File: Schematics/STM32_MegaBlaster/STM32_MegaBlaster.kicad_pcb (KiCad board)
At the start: 2 copper layers, 89 parts, among them J1 SD_Card, J2 USB_B, J3 Barrel_Jack, J4 AMP_OUT, J5 LINE_LEVEL_OUT, SW1 PREV, SW2 RAND, SW3 NEXT, SW4 OPTION, SW5 PWR_SWITCH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

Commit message: PCB near complete
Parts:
- removed J5: LINE_LEVEL_OUT, Connectors:PJ320E_3.5mm_Jack
- removed R12, R14: 9.1k, Resistors_THT:R_Axial_DIN0207_L6.3mm_D2.5mm_P7.62mm_Horizontal
- removed R13, R15: 1.2k, Resistors_THT:R_Axial_DIN0207_L6.3mm_D2.5mm_P7.62mm_Horizontal
- removed SW7: GLOBAL_MUTE, Switches:1825115-1
- added ?: , , F.Cu at (186.3, 47.1)
- added C37: 1000uF, Capacitors_THT:CP_Radial_D8.0mm_P2.50mm, F.Cu at (125.1, 36.2)
- added RV1: POT_Dual, Potentiometers:Potentiometer_Alps_RK163_Double_Vertical, F.Cu at (191.6, 116.6)
- C3: footprint Capacitors_THT:C_Axial_L22.0mm_D10.5mm_P27.50mm_Horizontal -> Capacitors_THT:C_Disc_D3.0mm_W1.6mm_P2.50mm
- SW5: value PWR_SWITCH -> POWER
- SW6: value MUTE_SN -> MUTE PSG
- moved C9 144.3 mm to (63.5, 71.8), turned to 180 degrees
- moved SW1 141.7 mm to (84.3, 101.7)
- moved C10 140.8 mm to (85.1, 78.7), turned to 270 degrees
- moved U4 135.2 mm to (69.8, 74.3)
- moved C4 133.2 mm to (105.4, 33.7), turned to 180 degrees
- moved U5 129.6 mm to (108.0, 37.5)
- moved R2 126.8 mm to (87.9, 38.7)
- moved R3 126.7 mm to (87.9, 35.4)
- moved C1 124.7 mm to (118.7, 38.7)
- moved C2 122.7 mm to (113.7, 38.7)
- moved C15 118.8 mm to (115.6, 33.7), turned to 180 degrees
- moved C12 118.7 mm to (63.5, 76.8), turned to 180 degrees
- moved C13 116.5 mm to (175.3, 43.2)
- moved J2 112.9 mm to (74.9, 88.3), turned to 180 degrees
- moved C16 110.2 mm to (128.9, 62.2), turned to 180 degrees
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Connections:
- J4 pad 1: GND -> Net-(J4-Pad1)
- J4 pad 2: L_OUT -> Net-(J4-Pad2)
- J4 pad 3: R_OUT -> Net-(J4-Pad3)
- J4 pad 4: Net-(J4-Pad4) -> GND
- U9 pad 3: Net-(SW7-Pad2) -> GND
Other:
- board outline added: 138.4 x 91.4 mm
- board text added: "I"
- board text added: "O"
- board text added: "OFF"
- board text added: "ON"

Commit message: PCB Complete
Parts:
- removed ?: , 
- added G***: LOGO, art:wave3, B.Cu at (154.1, 109.0)
- added G1: LOGO, art:wave1, F.Cu at (80.2, 112.3)
- added G2: LOGO, art:mega_blaster_logo, F.Cu at (71.4, 100.6)
- added G3: LOGO, art:wave2, B.Cu at (86.3, 106.0)
- added G4: LOGO, art:trees, B.Cu at (72.4, 47.8)
- SW6: value MUTE PSG -> MUTE_SN
- VOLUME: renamed from RV1; footprint Potentiometers:Potentiometer_Alps_RK163_Double_Vertical -> Potentiometer_Alps_RK163_Double_Vertical(SWAP)
- moved NEXT 10.8 mm to (116.0, 102.3)
- moved RAND 10.8 mm to (105.2, 102.3)
- moved PREV 10.8 mm to (95.0, 102.3)
- moved PLAYMODE 10.8 mm to (105.2, 111.7)
- moved J1 6.98 mm to (73.0, 48.3)
- moved C10 5.08 mm to (85.1, 73.7)
- moved C11 5.08 mm to (85.1, 68.6)
- moved Y1 5.08 mm to (80.0, 73.7)
- moved C9 3.81 mm to (63.5, 67.9)
- moved U4 3.81 mm to (69.8, 70.5)
- moved C12 3.81 mm to (63.5, 73.0)
- moved C3 2.29 mm to (113.0, 71.1)
- moved U2 2.01 mm to (116.2, 78.7)
- moved C16 1.91 mm to (130.8, 62.2)
- moved C5 1.91 mm to (125.7, 65.4)
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- renumbered SW3 to NEXT, SW4 to PLAYMODE, SW1 to PREV, SW2 to RAND
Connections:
- R3 pad 2: I2C_SCL -> I2C_SDA
- U1 pad 35: I2C_SCL -> I2C_SDA
- U12 pad 4: I2C_SCL -> I2C_SDA
- U5 pad 2: I2C_SCL -> I2C_SDA
- U6 pad 2: I2C_SCL -> I2C_SDA
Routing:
- net +5V: track 0.00 -> 234.1 mm, vias 0 -> 4
- net +3V3: track 0.00 -> 169.9 mm
- net GND: track 0.00 -> 107.3 mm, vias 0 -> 13
- net I2C_SDA: track 0.00 -> 95.2 mm, vias 0 -> 1
- net YM_A0: track 0.00 -> 94.8 mm, vias 0 -> 2
- net I2C_SCL: track 0.00 -> 91.8 mm
- net YM_WR: track 0.00 -> 87.3 mm
- net D6: track 0.00 -> 85.6 mm, vias 0 -> 1
- net D5: track 0.00 -> 85.1 mm, vias 0 -> 1
- net AGND: track 0.00 -> 85.0 mm
- net YM_A1: track 0.00 -> 73.7 mm, vias 0 -> 1
- net +12V: track 0.00 -> 73.2 mm
- net Net-(J1-Pad12): track 0.00 -> 71.8 mm
- net AVCC: track 0.00 -> 70.6 mm
- net D7: track 0.00 -> 67.7 mm, vias 0 -> 1
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- added copper zone on B.Cu, net GND
- added copper zone on F.Cu, net GND
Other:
- net class 12v added: clearance 0.2, trace_width 1, via_dia 0.8, via_drill 0.4
- net class 5v added: clearance 0.2, trace_width 0.5, via_dia 0.8, via_drill 0.4
- board text added: "*"
- board text added: "1.3" I2C OLED"
- board text added: "12V DC"
- board text added: "2018"
- board text added: "Aidan Lawrence www.aidanlawrence.com"
- board text added: "G N D"
- board text added: "PORT END"
- board text added: "S C L"
- board text added: "S D A"
- board text added: "Sega Genesis Video Game Music Player"
- board text added: "V C C"

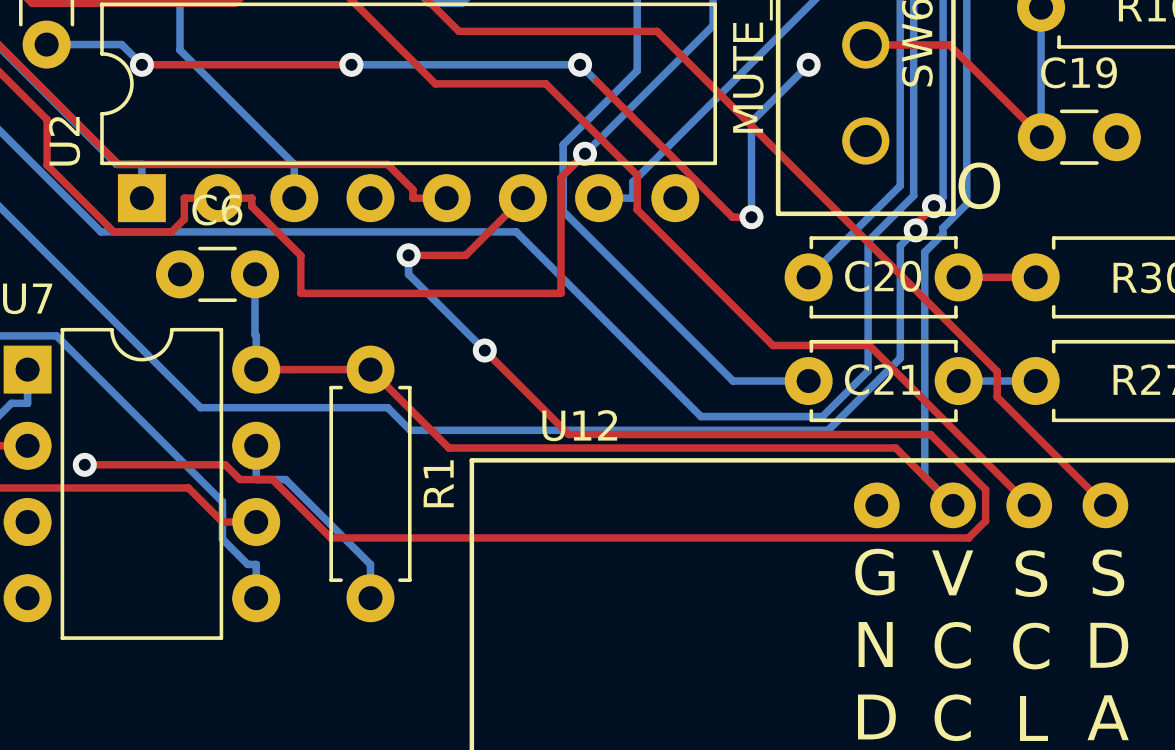
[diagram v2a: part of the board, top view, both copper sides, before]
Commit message: Moved gnd trace
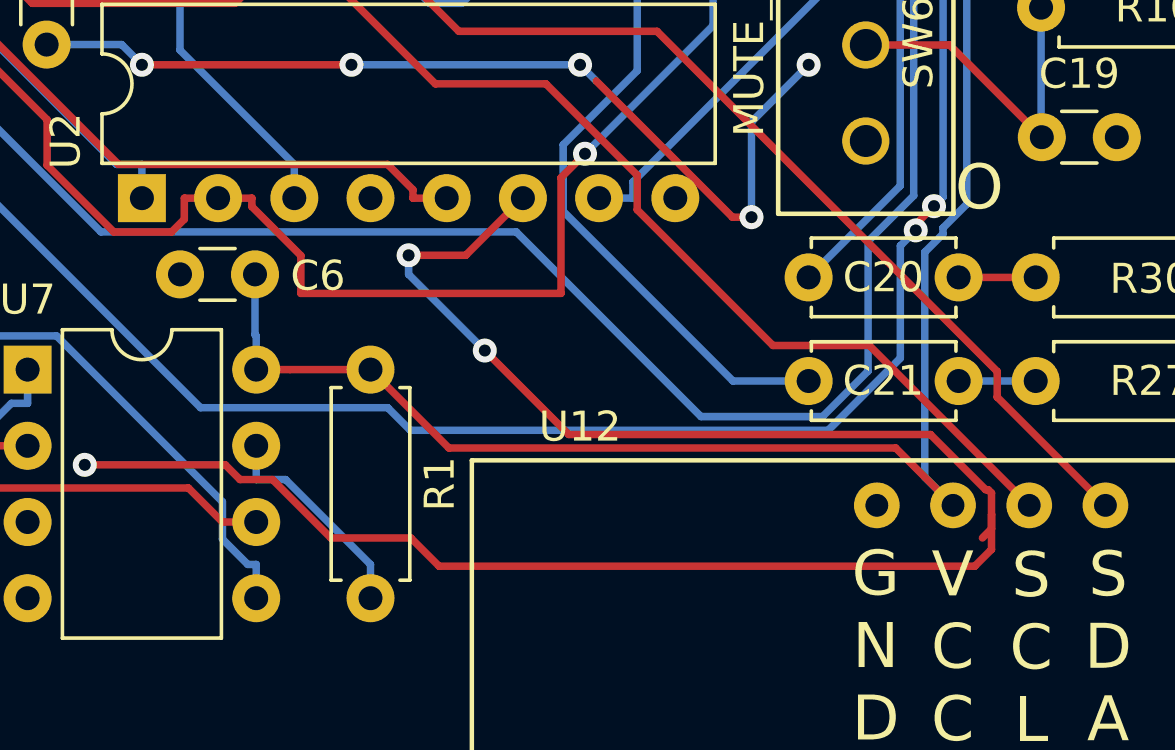
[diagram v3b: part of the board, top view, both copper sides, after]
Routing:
- net GND: track 107.3 -> 109.9 mm
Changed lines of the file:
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@@
     (thickness 1.6)
     (drawings 24)
-    (tracks 852)
+    (tracks 859)
     (zones 0)
     (modules 90)
@@
     (descr "C, Disc series, Radial, pin pitch=2.50mm, , diameter*width=3.0*1.6mm^2, Capacitor, http://www.vishay.com/docs/45233/krseries.pdf")
     (tags "C Disc series Radial pin pitch 2.50mm  diameter 3.0mm width 1.6mm Capacitor")
-    (fp_text reference C6 (at 1.25 -2.11) (layer F.SilkS)
+    (fp_text reference C6 (at 4.5974 0.0508) (layer F.SilkS)
       (effects (font (size 1 1) (thickness 0.15)))
     )
@@
   (via (at 114.3 87.63) (size 0.8) (drill 0.4) (layers F.Cu B.Cu) (net 4))
   (segment (start 118.984998 87.63) (end 114.3 87.63) (width 0.25) (layer F.Cu) (net 4))
+  (segment (start 119.474999 88.120001) (end 118.984998 87.63) (width 0.25) (layer F.Cu) (net 4))
   (segment (start 120.555001 88.120001) (end 119.474999 88.120001) (width 0.25) (layer F.Cu) (net 4))
+  (segment (start 122.502001 90.067001) (end 120.555001 88.120001) (width 0.25) (layer F.Cu) (net 4))
+  (segment (start 144.526 89.7636) (end 144.222599 90.067001) (width 0.25) (layer F.Cu) (net 4))
   (segment (start 130.43379 86.61879) (end 142.490552 86.61879) (width 0.25) (layer F.Cu) (net 4))
   (segment (start 127.635 83.82) (end 130.43379 86.61879) (width 0.25) (layer F.Cu) (net 4))
+  (segment (start 144.330001 88.458239) (end 144.414439 88.458239) (width 0.25) (layer F.Cu) (net 4))
+  (segment (start 144.414439 88.458239) (end 144.526 88.5698) (width 0.25) (layer F.Cu) (net 4))
   (segment (start 142.490552 86.61879) (end 144.330001 88.458239) (width 0.25) (layer F.Cu) (net 4))
-  (segment (start 122.502001 90.067001) (end 120.555001 88.120001) (width 0.25) (layer F.Cu) (net 4))
-  (segment (start 144.330001 88.458239) (end 144.330001 89.501761) (width 0.25) (layer F.Cu) (net 4))
-  (segment (start 144.330001 89.501761) (end 143.764761 90.067001) (width 0.25) (layer F.Cu) (net 4))
-  (segment (start 119.474999 88.120001) (end 118.984998 87.63) (width 0.25) (layer F.Cu) (net 4))
-  (segment (start 143.764761 90.067001) (end 122.502001 90.067001) (width 0.25) (layer F.Cu) (net 4))
+  (segment (start 144.526 89.281) (end 144.526 90.4494) (width 0.25) (layer F.Cu) (net 4))
+  (segment (start 144.526 89.281) (end 144.526 89.7636) (width 0.25) (layer F.Cu) (net 4))
+  (segment (start 144.526 88.5698) (end 144.526 89.281) (width 0.25) (layer F.Cu) (net 4))
+  (segment (start 144.526 90.4494) (end 143.9672 91.0082) (width 0.25) (layer F.Cu) (net 4))
+  (segment (start 143.9672 91.0082) (end 126.111 91.0082) (width 0.25) (layer F.Cu) (net 4))
+  (segment (start 125.169801 90.067001) (end 122.502001 90.067001) (width 0.25) (layer F.Cu) (net 4))
+  (segment (start 126.111 91.0082) (end 125.169801 90.067001) (width 0.25) (layer F.Cu) (net 4))
   (segment (start 143.243 88.98) (end 142.3005 88.0375) (width 0.25) (layer B.Cu) (net 5))
   (segment (start 142.3005 88.0375) (end 142.3005 80.5402) (width 0.25) (layer B.Cu) (net 5))

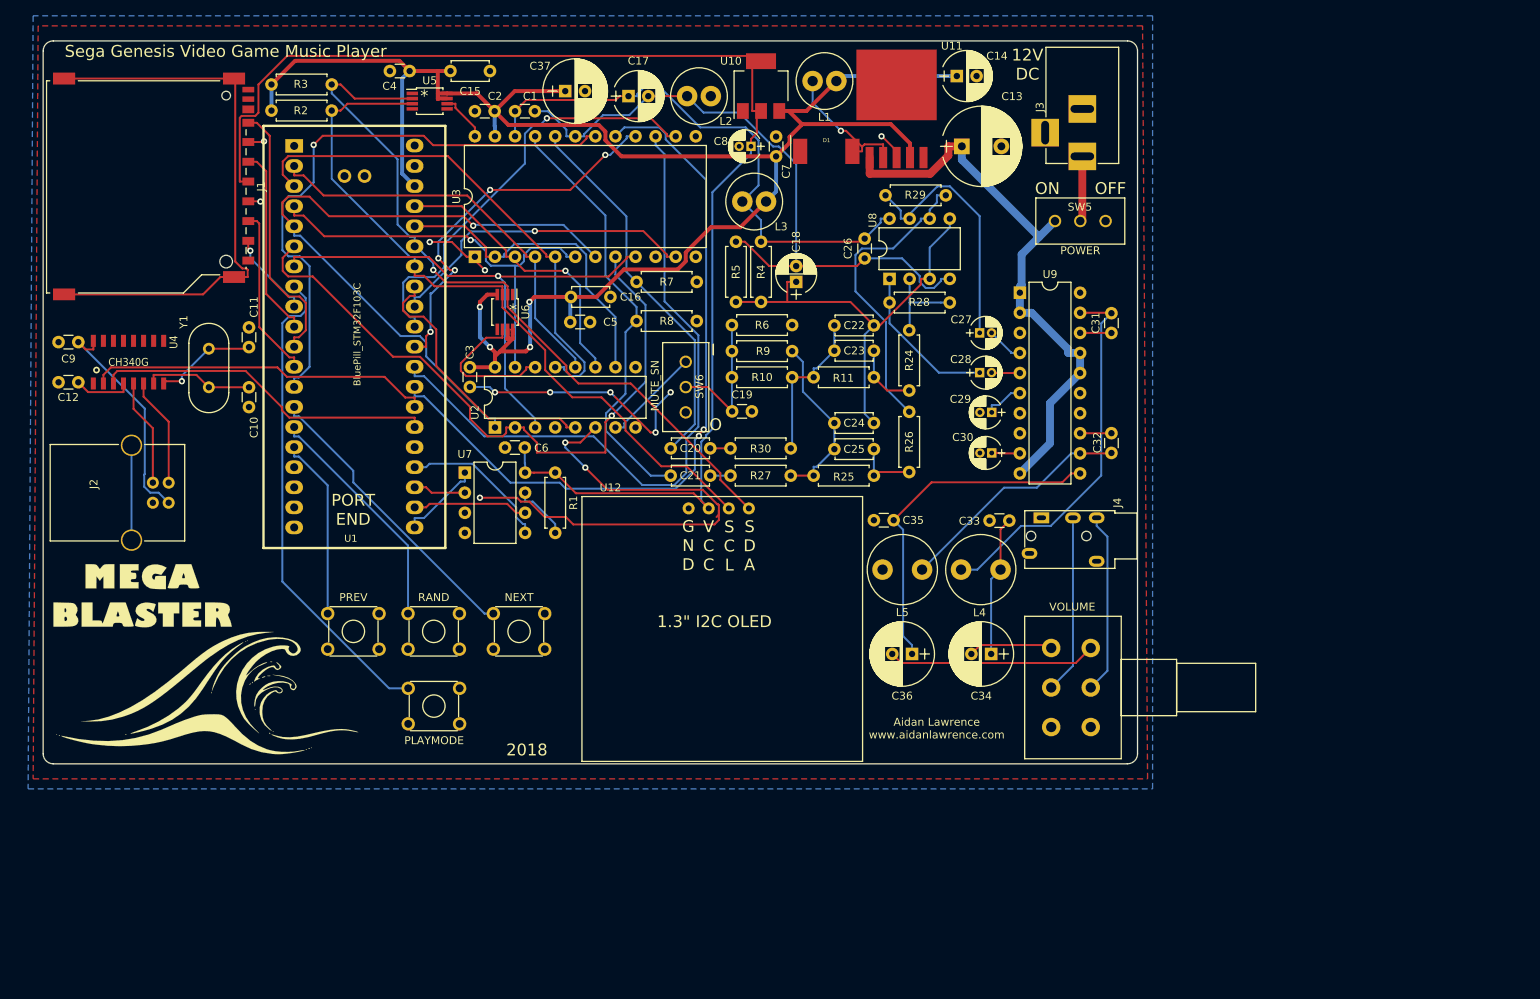
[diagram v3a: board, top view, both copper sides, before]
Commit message: Correct amplifier circuit and changed a couple footprints
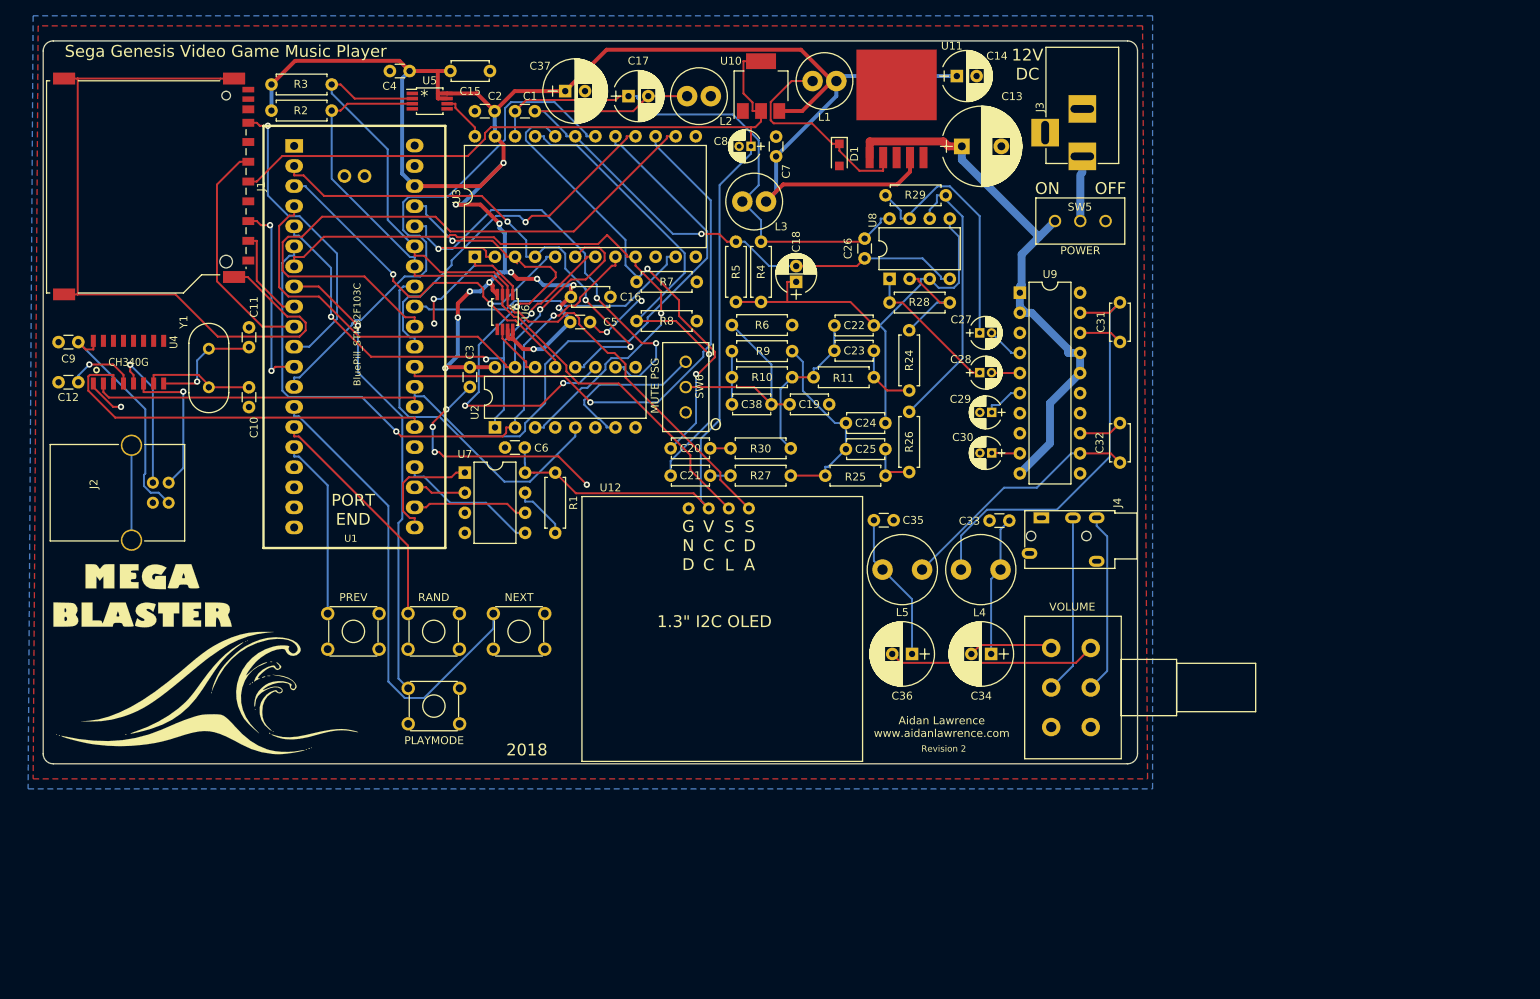
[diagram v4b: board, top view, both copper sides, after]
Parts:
- added C38: 1uF, Capacitors_THT:C_Disc_D4.7mm_W2.5mm_P5.00mm, F.Cu at (146.2, 75.8)
- C19, C31, C32: footprint Capacitors_THT:C_Disc_D3.0mm_W1.6mm_P2.50mm -> Capacitors_THT:C_Disc_D4.7mm_W2.5mm_P5.00mm
- D1: value SS34 -> SS34FACT-ND; footprint Diodes:DO-214AB -> Diodes_SMD:D_SOD-123F
- SW6: value MUTE_SN -> MUTE PSG
- moved C19 7.33 mm to (153.5, 75.8)
- moved C31 1.74 mm to (195.3, 62.9)
- moved D1 1.71 mm to (159.8, 44.3), turned to 270 degrees
- moved C32 1.63 mm to (195.3, 83.2)
- moved R25 1.47 mm to (165.6, 84.8)
- moved C24 1.46 mm to (165.6, 78.2)
- moved C25 1.46 mm to (165.6, 81.5)
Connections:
- C35 pad 1: GND -> Net-(C35-Pad1)
- C35 pad 2: Net-(C35-Pad2) -> GND
- C36 pad 1: Net-(C35-Pad2) -> Net-(C35-Pad1)
- J4 pad 1: Net-(J4-Pad1) -> GND
- J4 pad 4: GND -> (no net)
- L5 pad 2: GND -> Net-(C35-Pad1)
- R10 pad 2: Net-(C19-Pad1) -> Net-(C38-Pad1)
- R9 pad 2: Net-(C19-Pad1) -> Net-(C38-Pad1)
- SW6 pad 3: GND -> Net-(SW6-Pad3)
- U11 pad 6: (no net) -> GND
- U9 pad 11: Net-(C35-Pad2) -> GND
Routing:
- net GND: track 109.9 -> 64.2 mm, vias 13 -> 9
- net Net-(C35-Pad2): track 43.9 -> 0.00 mm
- net +5V: track 234.1 -> 261.4 mm, vias 4 -> 12
- net D1: track 37.2 -> 64.1 mm, vias 1 -> 4
- net YM_CS: track 54.6 -> 80.9 mm, vias 1 -> 0
- net Net-(J1-Pad12): track 71.8 -> 94.3 mm
- net NEXT: track 37.6 -> 59.7 mm
- net YM_A0: track 94.8 -> 74.1 mm, vias 2 -> 0
- net D0: track 41.2 -> 60.7 mm, vias 0 -> 3
- net D5: track 85.1 -> 65.6 mm, vias 1 -> 3
- net Net-(C35-Pad1): track 0.00 -> 18.9 mm
- net D4: track 55.0 -> 70.4 mm
- net YM_WR: track 87.3 -> 72.7 mm, vias 0 -> 1
- net D2: track 52.2 -> 65.2 mm, vias 0 -> 3
- net D7: track 67.7 -> 79.6 mm
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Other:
- board text added: "Revision 2"
